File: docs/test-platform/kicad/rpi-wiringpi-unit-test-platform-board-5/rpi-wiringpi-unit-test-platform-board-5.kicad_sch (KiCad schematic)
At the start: 13 parts, among them J1 JST_IN_PWR, J2 JST_IN_SIG, J3 JST_IN_LCD, J4 JST_OUT_ARDUINO, SW1 SW_DIP_x03, U1 LVLSHIFT

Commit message: Updated boards
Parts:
- added R2: 220, Resistor_THT:R_Axial_DIN0207_L6.3mm_D2.5mm_P7.62mm_Horizontal, symbol Device:R
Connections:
- net +3V3: no longer C1.1, C3.1
- net +5V: now also C1.1, C3.1
- net LCD_BL_A: now also R2.2; no longer LCD1.15 (A)
- new net: LCD1.15 (A), R2.1
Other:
- moved on the sheet: C1, C2, C3

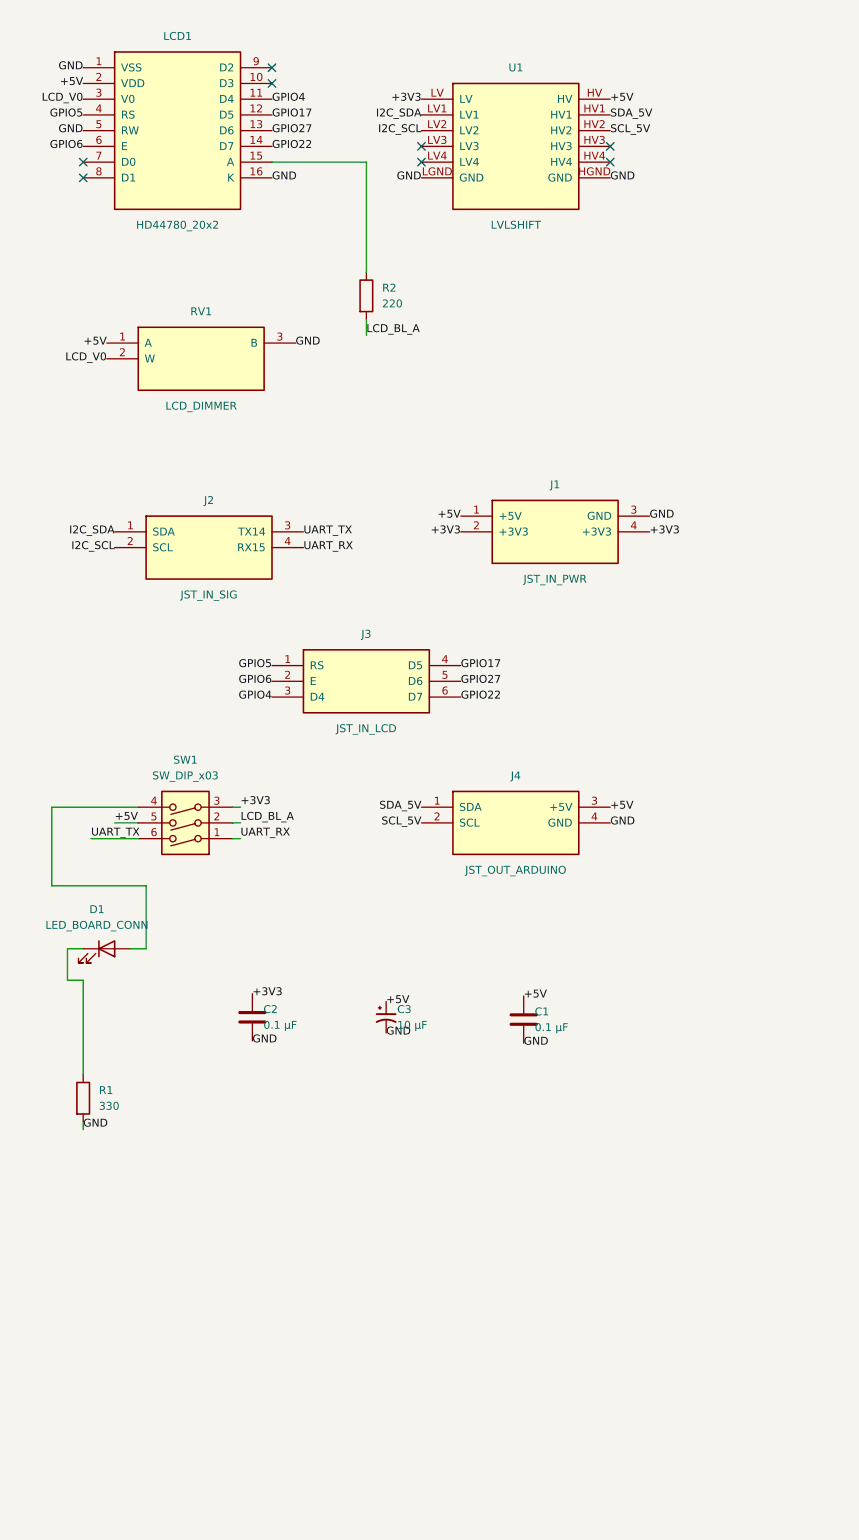
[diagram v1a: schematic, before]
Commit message: Add test file for PCA9685 PWM IC; work on board 5
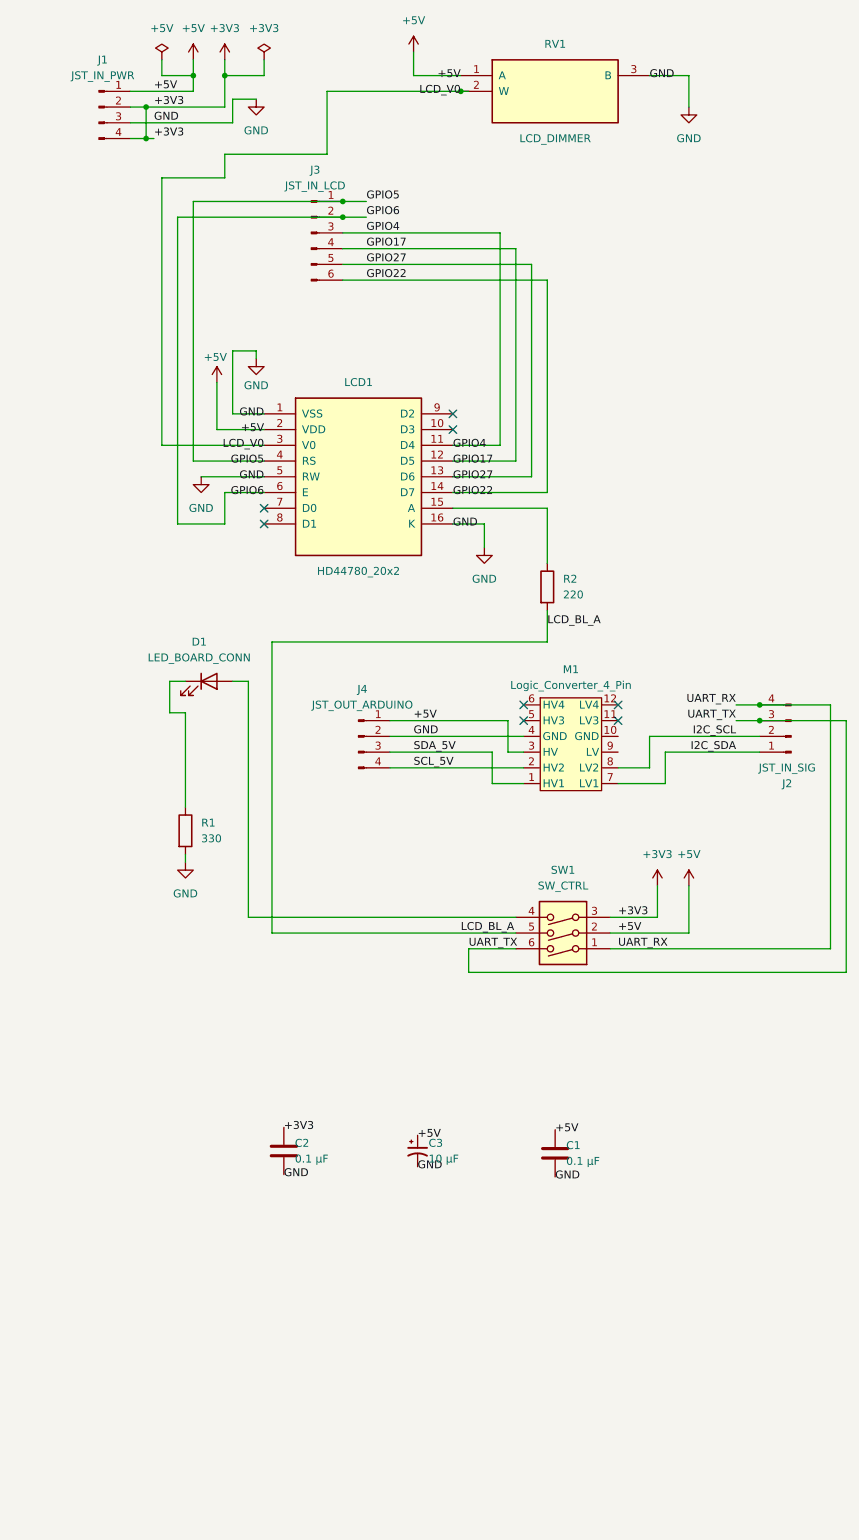
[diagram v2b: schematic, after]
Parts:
- removed J1: JST_IN_PWR, rpi-wiringpi-unit-test-platform-board-5:J1, symbol rpi-wiringpi-unit-test-platform-board-5:J1
- removed J2: JST_IN_SIG, rpi-wiringpi-unit-test-platform-board-5:J2, symbol rpi-wiringpi-unit-test-platform-board-5:J2
- removed J3: JST_IN_LCD, rpi-wiringpi-unit-test-platform-board-5:J3, symbol rpi-wiringpi-unit-test-platform-board-5:J3
- removed J4: JST_OUT_ARDUINO, rpi-wiringpi-unit-test-platform-board-5:J4, symbol rpi-wiringpi-unit-test-platform-board-5:J4
- removed U1: LVLSHIFT, rpi-wiringpi-unit-test-platform-board-5:U1, symbol rpi-wiringpi-unit-test-platform-board-5:U1
- added J1: JST_IN_PWR, symbol Connector:Conn_01x04_Pin
- added J2: JST_IN_SIG, symbol Connector:Conn_01x04_Pin
- added J3: JST_IN_LCD, symbol Connector:Conn_01x06_Pin
- added J4: JST_OUT_ARDUINO, symbol Connector:Conn_01x04_Pin
- added M1: Logic_Converter_4_Pin, RPi:Level_Converter_4_Pin, symbol RPi:Level_Converter_4_Pin
- RV1: footprint rpi-wiringpi-unit-test-platform-board-5:RV1 -> Potentiometer_THT:Potentiometer_Alps_RK09K_Single_Vertical
- SW1: value SW_DIP_x03 -> SW_CTRL
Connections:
- net +3V3: now also J1.2 (Pin_2), J1.4 (Pin_4)
- net +5V: now also SW1.2, J1.1 (Pin_1), J4.1 (Pin_1), M1.3 (HV); no longer SW1.5
- net GND: now also J1.3 (Pin_3), J4.2 (Pin_2), M1.4 (GND)
- net GPIO17: now also J3.4 (Pin_4)
- net GPIO22: now also J3.6 (Pin_6)
- net GPIO27: now also J3.5 (Pin_5)
- net GPIO4: now also J3.3 (Pin_3)
- net GPIO5: now also J3.1 (Pin_1)
- net GPIO6: now also J3.2 (Pin_2)
- net I2C_SCL: now also J2.2 (Pin_2), M1.8 (LV2)
- net I2C_SDA: now also J2.1 (Pin_1), M1.7 (LV1)
- net LCD_BL_A: now also SW1.5; no longer SW1.2
- net SCL_5V: now also J4.4 (Pin_4), M1.2 (HV2)
- net SDA_5V: now also J4.3 (Pin_3), M1.1 (HV1)
- net UART_RX: now also J2.4 (Pin_4)
- net UART_TX: now also J2.3 (Pin_3)
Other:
- moved on the sheet: C1, C2, C3, D1, LCD1, R1, R2, RV1, SW1

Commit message: Cleanup
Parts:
- J1, J2, J4: footprint (none) -> Connector_JST:JST_XH_B4B-XH-A_1x04_P2.50mm_Vertical
- J3: footprint (none) -> Connector_JST:JST_XH_B6B-XH-A_1x06_P2.50mm_Vertical
- LCD1: footprint rpi-wiringpi-unit-test-platform-board-5:LCD1 -> RPi:HD44780_LCD_Module
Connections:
- net +3V3: now also SW1.6; no longer SW1.3
- net +5V: now also SW1.5; no longer SW1.2
- net LCD_BL_A: now also SW1.2; no longer SW1.5
- net UART_RX: now also SW1.4; no longer SW1.1
- net UART_TX: now also SW1.3; no longer SW1.6
- net at D1.2 (A): now also SW1.1; no longer SW1.4
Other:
- moved on the sheet: SW1
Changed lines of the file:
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@@
 			)
 		)
-		(property "Footprint" ""
+		(property "Footprint" "Connector_JST:JST_XH_B4B-XH-A_1x04_P2.50mm_Vertical"
 			(at 67.31 130.81 0)
 			(hide yes)
@@
 	(symbol
 		(lib_id "Switch:SW_DIP_x03")
-		(at 100.33 162.56 180)
+		(at 100.33 162.56 0)
 		(unit 1)
 		(body_style 1)
@@
 		)
 		(property "Footprint" "Button_Switch_THT:SW_DIP_SPSTx03_Slide_9.78x9.8mm_W7.62mm_P2.54mm"
-			(at 100.33 160.02 0)
-			(hide yes)
-			(show_name no)
-			(do_not_autoplace no)
-			(effects
-				(font
-					(size 1.27 1.27)
-				)
-			)
-		)
-		(property "Datasheet" ""
-			(at 100.33 160.02 0)
+			(at 100.33 165.1 0)
+			(hide yes)
+			(show_name no)
+			(do_not_autoplace no)
+			(effects
+				(font
+					(size 1.27 1.27)
+				)
+			)
+		)
+		(property "Datasheet" ""
+			(at 100.33 165.1 0)
 			(hide yes)
 			(show_name no)
@@
 			)
 		)
-		(property "Footprint" ""
+		(property "Footprint" "Connector_JST:JST_XH_B4B-XH-A_1x04_P2.50mm_Vertical"
 			(at 137.16 130.81 0)
 			(hide yes)
@@
 			)
 		)
-		(property "Footprint" ""
+		(property "Footprint" "Connector_JST:JST_XH_B6B-XH-A_1x06_P2.50mm_Vertical"
 			(at 59.69 49.53 0)
 			(hide yes)
@@
 			)
 		)
-		(property "Footprint" ""
+		(property "Footprint" "Connector_JST:JST_XH_B4B-XH-A_1x04_P2.50mm_Vertical"
 			(at 25.4 29.21 0)
 			(hide yes)
@@
 			)
 		)
-		(property "Footprint" "rpi-wiringpi-unit-test-platform-board-5:LCD1"
+		(property "Footprint" "RPi:HD44780_LCD_Module"
 			(at 67.31 88.9 0)
 			(hide yes)

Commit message: Finished test board 5
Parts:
- removed LCD1: HD44780_20x2, RPi:HD44780_LCD_Module, symbol rpi-wiringpi-unit-test-platform-board-5:LCD1
- removed RV1: LCD_DIMMER, Potentiometer_THT:Potentiometer_Alps_RK09K_Single_Vertical, symbol rpi-wiringpi-unit-test-platform-board-5:RV1
- added C4: 10 µF, Capacitor_THT:CP_Radial_D5.0mm_P2.50mm, symbol Device:C_Polarized_Small_US
- added RV1: LCD_DIMMER, Potentiometer_THT:Potentiometer_Alps_RK09K_Single_Vertical, symbol Device:R_Potentiometer
- added U1: LCD_HD44780, RPi:HD44780_LCD_Module, symbol RPi:LCD_HD44780
- D1: value LED_BOARD_CONN -> LED_BRD_CONN
- M1: value Logic_Converter_4_Pin -> Logic_Lvl_Shifter
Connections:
- net +3V3: now also M1.9 (LV)
- net +5V: now also C4.1, RV1.1, U1.2 (VCC)
- net GND: now also M1.10 (GND), C4.2, RV1.3, U1.1 (GND), U1.16 (BL-C(-)), U1.5 (R/W)
- net GPIO17: now also U1.12 (D5)
- net GPIO22: now also U1.14 (D7)
- net GPIO27: now also U1.13 (D6)
- net GPIO4: now also U1.11 (D4)
- net GPIO5: now also U1.4 (RS)
- net GPIO6: now also U1.6 (EN)
- net LCD_V0: now also RV1.2, U1.3 (Vo)
- net at R2.1: now also U1.15 (BL-A(+))
- net LED_BRD_CONN: now reaches D1.2 (A), SW1.1
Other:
- moved on the sheet: C1, C2, C3, J2, J4, M1, R1, R2, SW1
